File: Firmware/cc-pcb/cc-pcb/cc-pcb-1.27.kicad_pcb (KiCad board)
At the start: 2 copper layers, 39.4 x 36.8 mm, 21 parts, among them CON1 BARREL_JACK, IC1 ATMEGA328P-A, P1 CONN_6, P2 CONN_6, P3 CONN_8, P4 CONN_2, P5 CONN_6, P6 CONN_6, SW1 SRS

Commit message: Working on 1.27mm 10x2 pin socket
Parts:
- removed P2: CONN_6, pin_strip_1.27mm_4x2_90
- removed P3: CONN_8, pin_strip_1.27mm_4x2_90
- P1: value CONN_6 -> CONN_20; footprint pin_strip_1.27mm_4x2_90 -> pin_strip_1.27mm_10x2_90
- moved P1 7.35 mm to (185.2, 87.1)
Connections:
- IC1 pad 1: N-0000016 -> N-0000012
- IC1 pad 10: N-0000013 -> N-000009
- IC1 pad 11: N-0000012 -> N-000008
- IC1 pad 2: N-0000015 -> N-0000011
- IC1 pad 23: N-0000022 (its old number) -> N-0000016
- IC1 pad 24: N-0000021 (its old number) -> N-0000015
- IC1 pad 25: N-0000020 (its old number) -> N-0000014
- IC1 pad 26: N-0000019 (its old number) -> N-0000031
- IC1 pad 27: N-0000018 (its old number) -> N-0000030
- IC1 pad 28: N-0000017 (its old number) -> N-0000029
- IC1 pad 30: N-0000025 (its old number) -> N-000005
- IC1 pad 31: N-000002 (its old number) -> N-000006
- IC1 pad 32: N-000001 (its old number) -> N-0000013
- IC1 pad 9: N-0000014 -> N-0000010
- P1 pad 7: (no net) -> N-0000016
- P1 pad 8: (no net) -> N-0000015
- P5 pad 2: N-000002 (its old number) -> N-000006
- P5 pad 3: N-0000025 (its old number) -> N-000005
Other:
- outline, holes or cut-outs redrawn

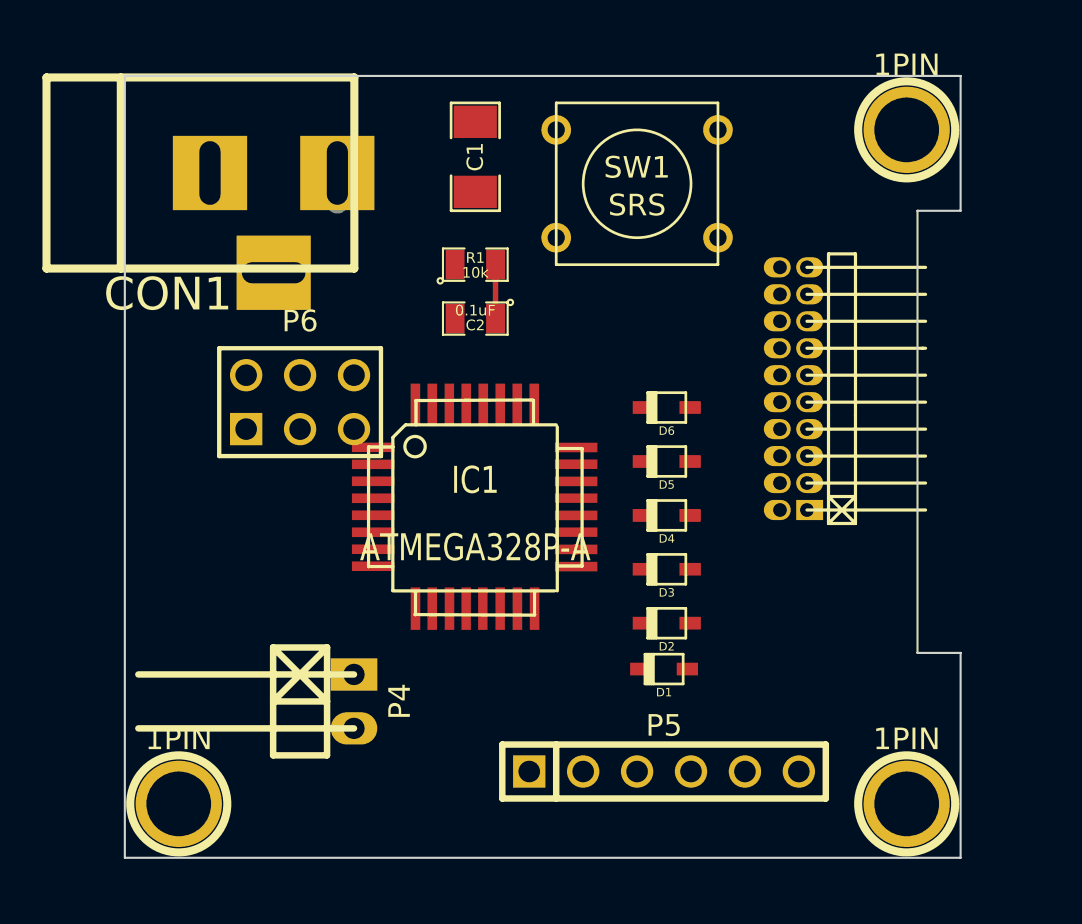
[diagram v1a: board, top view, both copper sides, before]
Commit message: Working on 1.27mm 10x2 pin socket PCB
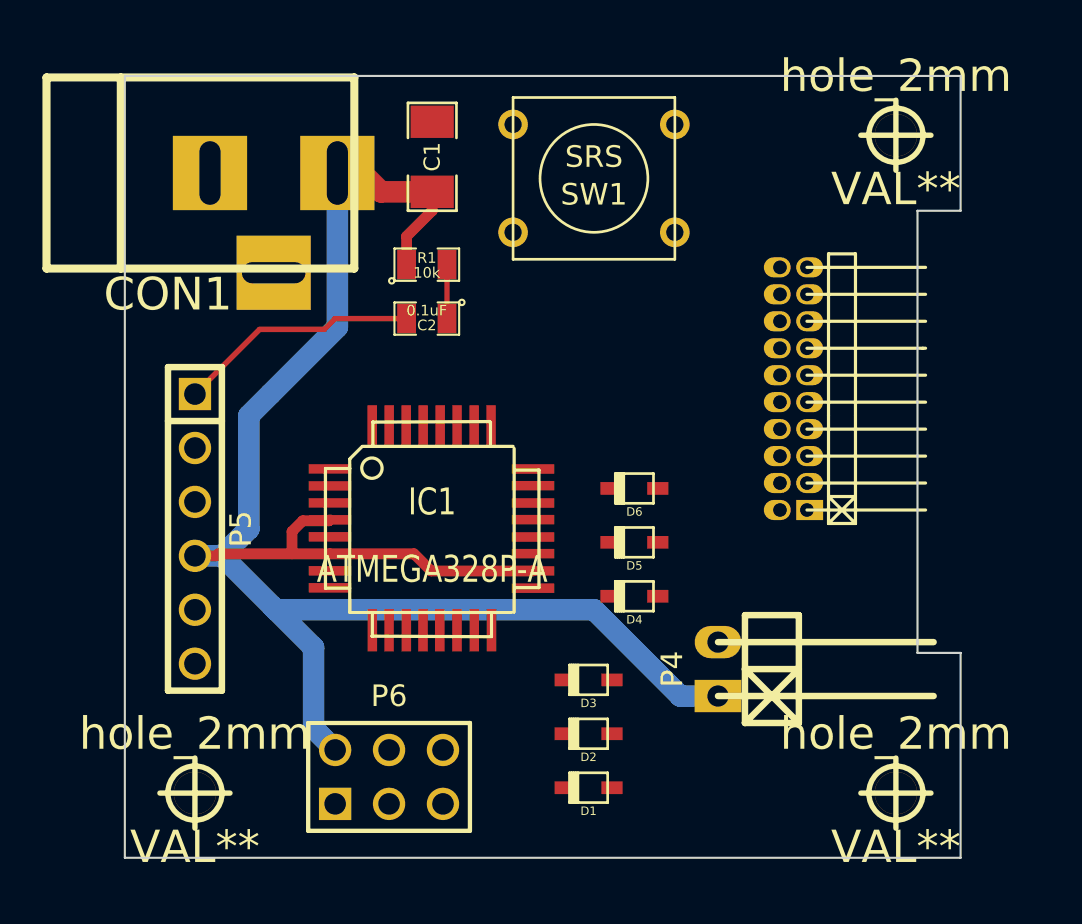
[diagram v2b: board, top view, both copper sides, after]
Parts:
- removed 1PIN (x3): P***, 1pin
- added hole_2mm: VAL**, hole_2mm, F.Cu at (190.0, 75.2)
- added hole_2mm: VAL**, hole_2mm, F.Cu at (190.0, 106.2)
- added hole_2mm: VAL**, hole_2mm, F.Cu at (157.0, 106.2)
- moved P5 24.9 mm to (157.0, 93.7), turned to 270 degrees
- moved P6 18.1 mm to (166.1, 105.4)
- moved P4 17.2 mm to (181.6, 100.3), turned to 90 degrees
- moved D1 6.62 mm to (175.5, 105.9)
- moved D2 6.38 mm to (175.5, 103.4)
- moved D3 6.38 mm to (175.5, 100.8)
- moved D4 4.10 mm to (177.7, 96.9)
- moved D5 4.10 mm to (177.7, 94.4)
- moved D6 4.10 mm to (177.7, 91.8)
- moved C2 2.29 mm to (167.9, 83.8)
- moved R1 2.29 mm to (167.9, 81.3)
- moved IC1 2.27 mm to (168.1, 93.7)
- moved SW1 2.05 mm to (175.8, 77.2), turned to 180 degrees
- moved C1 2.03 mm to (168.1, 76.2)
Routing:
- net VCC: track 2.82 -> 83.7 mm
- net N-000004: track 0.00 -> 11.4 mm

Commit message: Removed FreeRouting from the repo
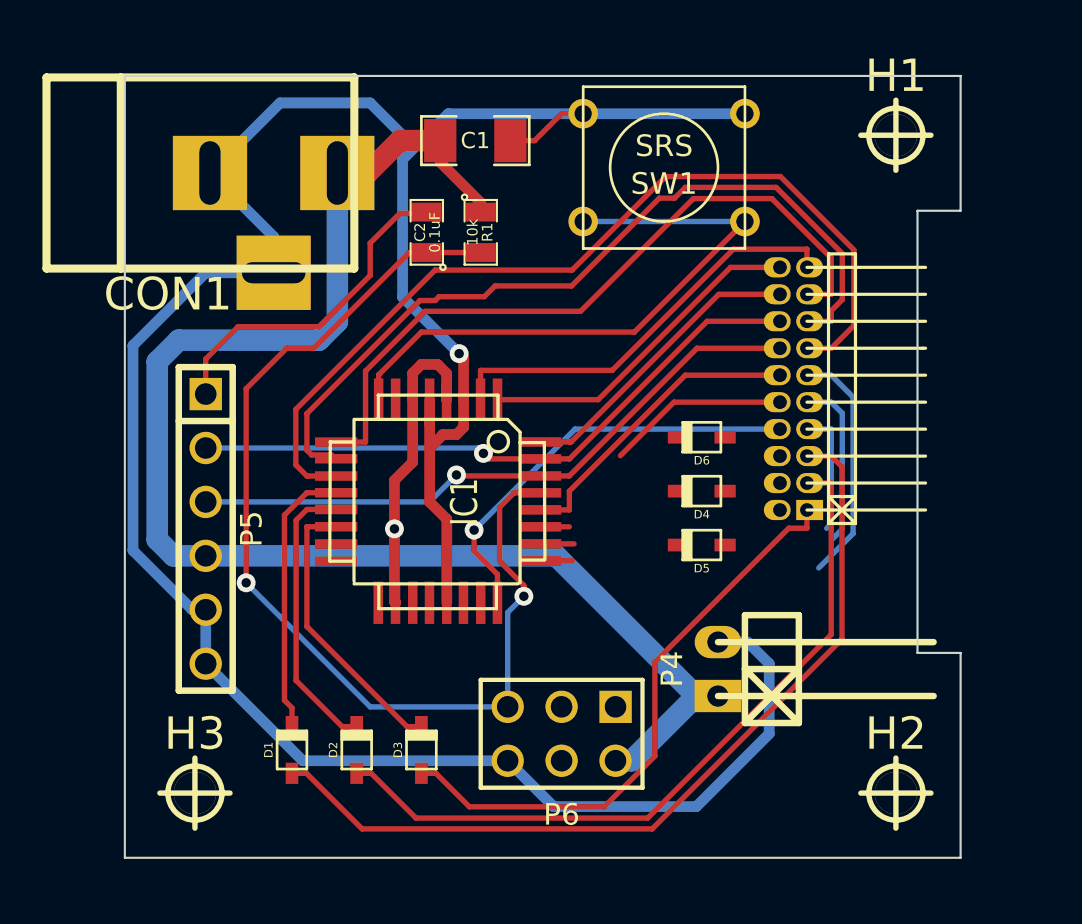
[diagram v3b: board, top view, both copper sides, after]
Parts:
- H1, H2, H3: renamed from hole_2mm; value VAL** -> (none)
- IC1: value ATMEGA328P-A -> (none)
- moved D1 14.1 mm to (161.5, 104.1), turned to 90 degrees
- moved D2 10.9 mm to (164.6, 104.1), turned to 90 degrees
- moved D3 8.54 mm to (167.6, 104.1), turned to 90 degrees
- moved P6 8.38 mm to (174.2, 103.4), turned to 180 degrees
- moved D4 5.88 mm to (180.8, 91.9)
- moved C2 4.06 mm to (167.9, 79.8), turned to 90 degrees
- moved D6 3.99 mm to (180.8, 89.4)
- moved SW1 3.34 mm to (179.1, 76.7)
- moved D5 3.18 mm to (180.8, 94.5)
- moved R1 2.96 mm to (170.4, 79.8), turned to 270 degrees
- moved C1 2.17 mm to (170.2, 75.4), turned to 0 degrees
- moved IC1 1.30 mm to (168.4, 92.5), turned to 270 degrees
- moved P5 0.51 mm to (157.5, 93.7)
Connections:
- D1 pad 1: N-0000026 (its old number) -> N-0000022
- D2 pad 1: N-0000025 -> N-0000021
- D5 pad 1: N-0000022 -> N-0000025
- IC1 pad 30: N-000005 (its old number) -> N-000004
- IC1 pad 31: N-000006 -> N-000001
- IC1 pad 32: N-0000013 (its old number) -> N-000003
- P1 pad 1: N-0000026 (its old number) -> N-0000024
- P1 pad 13: N-000005 (its old number) -> N-000008
- P1 pad 14: N-000006 -> N-000004
- P1 pad 15: N-0000013 (its old number) -> N-000009
- P1 pad 16: N-0000012 -> N-000001
- P1 pad 17: N-0000011 -> N-0000010
- P1 pad 18: N-0000010 -> N-000003
- P1 pad 19: N-000009 -> N-0000011
- P1 pad 20: N-000008 -> N-0000012
- P1 pad 3: N-0000024 -> N-0000021
- P5 pad 2: N-000006 -> N-000001
- P5 pad 3: N-000005 (its old number) -> N-000004
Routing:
- net GND: track 0.00 -> 127.7 mm, vias 0 -> 1
- net N-0000016: track 2.54 -> 50.9 mm, vias 0 -> 2
- net N-000008: track 0.00 -> 43.2 mm
- net N-0000022: track 0.00 -> 40.7 mm
- net N-000009: track 0.00 -> 38.8 mm
- net N-0000021: track 0.00 -> 35.1 mm
- net N-0000010: track 0.00 -> 34.0 mm
- net N-000004: track 0.00 -> 30.1 mm, vias 0 -> 1
- net N-000001: track 0.00 -> 29.9 mm, vias 0 -> 1
- net N-000005: track 0.00 -> 29.6 mm
- net N-0000024: track 0.00 -> 27.7 mm
- net N-0000030: track 0.00 -> 20.3 mm, vias 0 -> 1
- net N-0000011: track 0.01 -> 20.0 mm
- net N-0000012: track 0.00 -> 15.9 mm
- net N-0000027: track 0.00 -> 14.4 mm
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
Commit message: First PCB
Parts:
- IC1: value (none) -> ATMEGA328P-A
- moved D4 3.56 mm to (180.8, 95.5)
- moved D5 1.52 mm to (180.8, 93.0)
- moved D6 1.02 mm to (180.8, 90.4)
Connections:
- D4 pad 1: N-0000020 -> N-0000024
- D5 pad 1: N-0000025 -> N-0000023
- IC1 pad 23: N-0000031 (its old number) -> N-0000028
- IC1 pad 24: N-0000030 (its old number) -> N-0000027
- IC1 pad 25: N-0000029 (its old number) -> N-0000022
- IC1 pad 26: N-0000026 (its old number) -> N-0000021
- IC1 pad 27: N-0000028 -> N-0000020
- P1 pad 10: N-0000026 (its old number) -> N-0000020
- P1 pad 2: N-0000025 -> N-0000024
- P1 pad 4: N-0000020 -> N-0000023
- P1 pad 7: N-0000031 (its old number) -> N-0000022
- P1 pad 8: N-0000030 (its old number) -> N-0000021
- P1 pad 9: N-0000029 (its old number) -> N-0000027
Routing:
- net N-0000012: track 0.00 -> 38.6 mm
- net N-0000014: track 0.00 -> 29.4 mm
- net N-0000013: track 0.00 -> 25.7 mm
- net N-0000027: track 0.00 -> 25.0 mm, vias 0 -> 1
- net N-0000022: track 0.00 -> 20.6 mm, vias 0 -> 1
- net N-0000030 (its old number): track 20.3 -> 0.00 mm, vias 1 -> 0
- net N-0000028: track 12.7 -> 29.8 mm, vias 0 -> 1
- net N-0000021: track 0.00 -> 14.3 mm
- net N-0000020: track 0.00 -> 14.3 mm
- net N-0000026 (its old number): track 10.2 -> 0.00 mm
- net N-0000029 (its old number): track 9.57 -> 0.00 mm
- net N-0000031 (its old number): track 5.90 -> 0.00 mm
- net N-0000015: track 50.9 -> 56.0 mm, vias 2 -> 3
- net N-0000024: track 0.00 -> 3.91 mm
- net N-0000023: track 0.00 -> 3.16 mm
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
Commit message: without errors
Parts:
- CON1: value BARREL_JACK -> (none)
- D1, D2, D3, D4, D5, D6: value DIODE -> (none)
- IC1: value ATMEGA328P-A -> (none)
- P1: value CONN_20 -> (none)
- P4: value CONN_2 -> (none)
- P5, P6: value CONN_6 -> (none)
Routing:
- net GND: track 127.7 -> 23.0 mm
- net N-000009: track 34.0 -> 33.2 mm
- net N-0000011: track 15.9 -> 16.6 mm
- net N-000005: track 29.6 -> 30.2 mm

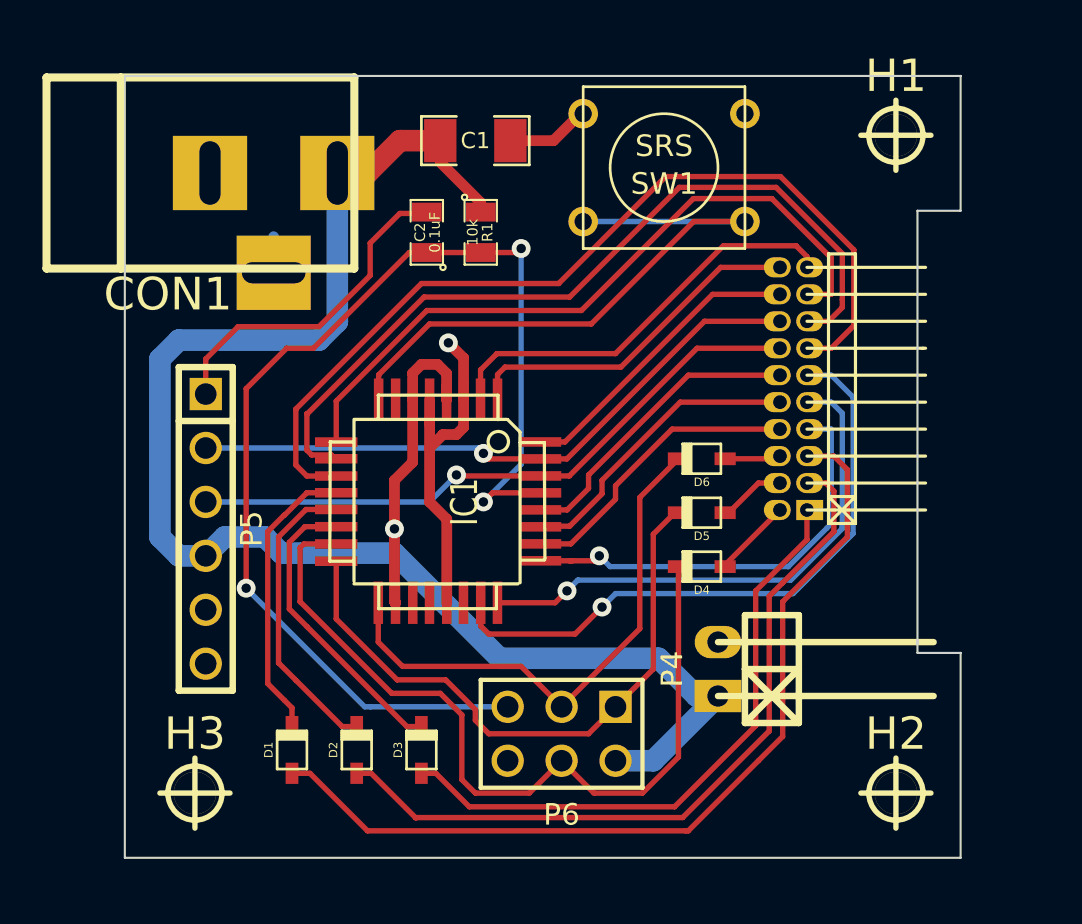
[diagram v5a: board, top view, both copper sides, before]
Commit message: Rectified PCB, added filled areas
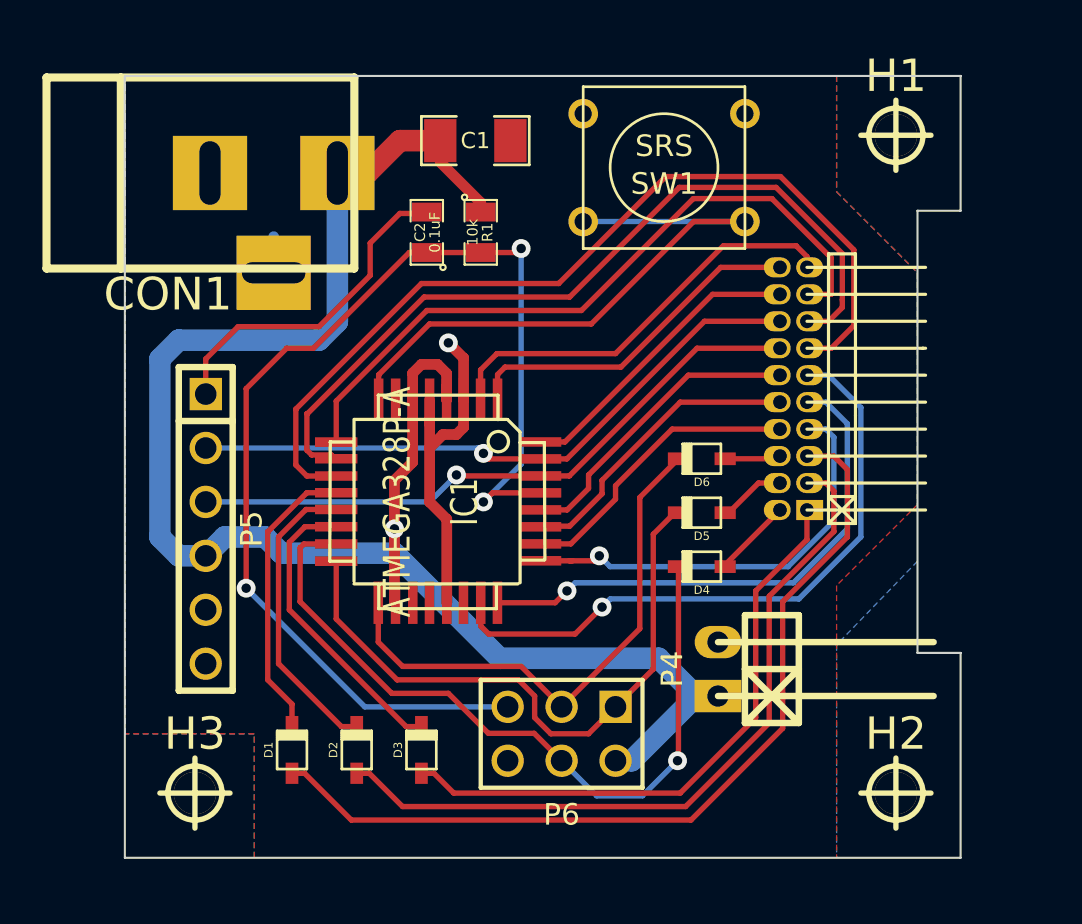
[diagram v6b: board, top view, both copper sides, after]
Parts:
- CON1: value (none) -> BARREL_JACK
- D1, D2, D3, D4, D5, D6: value (none) -> DIODE
- IC1: value (none) -> ATMEGA328P-A
- P1: value (none) -> CONN_20
- P4: value (none) -> CONN_2
- P5, P6: value (none) -> CONN_6
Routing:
- net GND: track 23.0 -> 19.1 mm
- net N-0000012: track 38.6 -> 35.7 mm, vias 0 -> 1
- net N-0000019: track 29.1 -> 28.4 mm
- net N-0000017: track 36.0 -> 35.3 mm
- net N-0000018: track 42.1 -> 41.4 mm
- net N-0000028: track 29.8 -> 30.3 mm
- added copper zone on B.Cu, net GND
- added copper zone on F.Cu, net GND
